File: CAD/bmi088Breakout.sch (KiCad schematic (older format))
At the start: 8 parts, among them J1 Conn_01x04_Male, U1 BMI088

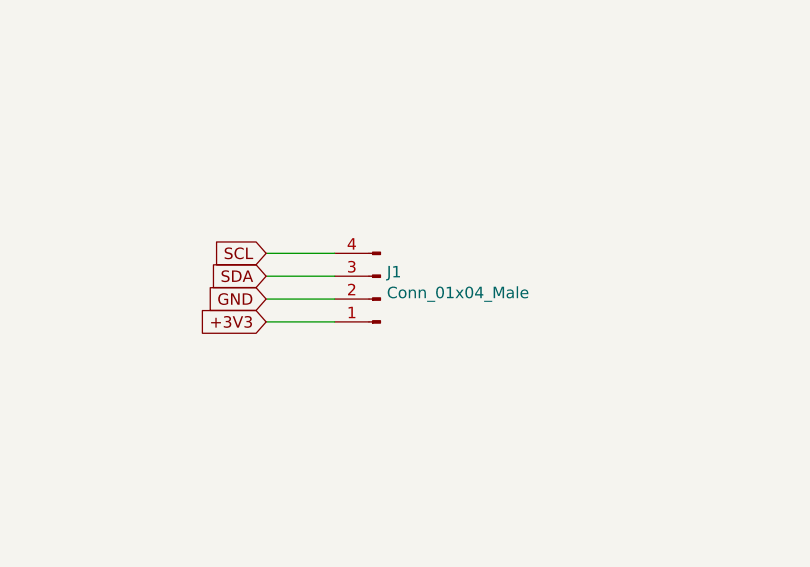
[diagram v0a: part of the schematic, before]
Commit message: added castellated holes to board
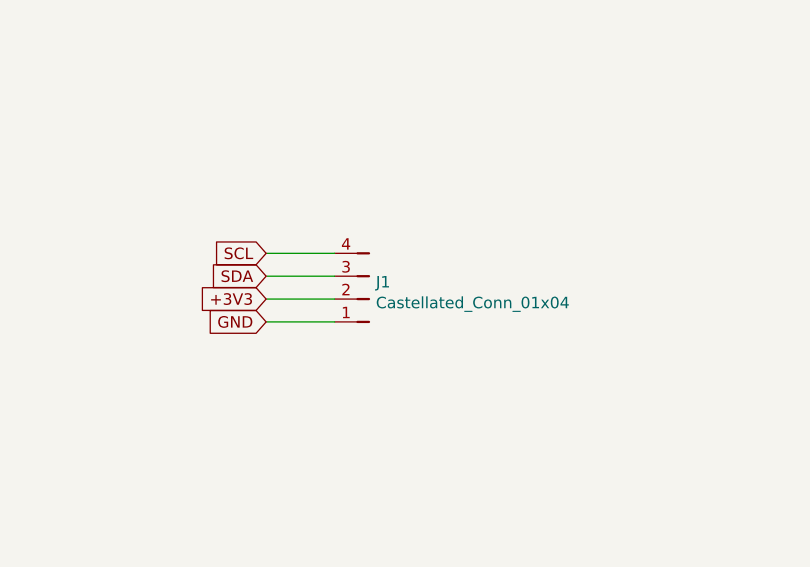
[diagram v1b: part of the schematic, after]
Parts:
- removed J1: Conn_01x04_Male, Connector_PinHeader_2.54mm:PinHeader_1x04_P2.54mm_Vertical, symbol Connector:Conn_01x04_Male
- added J1: Castellated_Conn_01x04, DS-connectors:Castellated_PinHeader_01x04_P2.54mm_Vertical, symbol DS-connectors:Castellated_Conn_01x04
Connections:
- net +3V3: now also J1.2
- net GND: now also J1.1
- net SCL: now also J1.4
- net SDA: now also J1.3
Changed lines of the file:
@@
 Wire Wire Line
 	6250 3150 6250 3300
-$Comp
-L Connector:Conn_01x04_Male J1
-U 1 1 614B0AD0
-P 6000 5050
-F 0 "J1" H 5972 4932 50  0000 R CNN
-F 1 "Conn_01x04_Male" H 5972 5023 50  0000 R CNN
-F 2 "Connector_PinHeader_2.54mm:PinHeader_1x04_P2.54mm_Vertical" H 6000 5050 50  0001 C CNN
-F 3 "~" H 6000 5050 50  0001 C CNN
-	1    6000 5050
-	-1   0    0    1
-$EndComp
 Text GLabel 5500 4850 0    50   Input ~ 0
 SCL
@@
 SDA
 Text GLabel 5500 5050 0    50   Input ~ 0
++3V3
+Text GLabel 5500 5150 0    50   Input ~ 0
 GND
-Text GLabel 5500 5150 0    50   Input ~ 0
-+3V3
 Wire Wire Line
 	5500 5150 5800 5150
@@
 Wire Wire Line
 	5500 4950 5800 4950
+$Comp
+L DS-connectors:Castellated_Conn_01x04 J1
+U 1 1 61534104
+P 5950 5200
+F 0 "J1" H 5920 4976 50  0000 R CNN
+F 1 "Castellated_Conn_01x04" H 5920 5067 50  0000 R CNN
+F 2 "DS-connectors:Castellated_PinHeader_01x04_P2.54mm_Vertical" H 5950 5200 50  0001 C CNN
+F 3 "" H 5950 5200 50  0001 C CNN
+	1    5950 5200
+	-1   0    0    1
+$EndComp
 $EndSCHEMATC

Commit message: Add files via upload
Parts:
- added J2, J3: Castellated_Conn_01x01, DS-connectors:Castellated_PinHeader_01x01_P2.54mm_Vertical, symbol DS-connectors:Castellated_Conn_01x01
- C1, C2: footprint Capacitor_SMD:C_0603_1608Metric -> Capacitor_SMD:C_0805_2012Metric
- R1, R2, R3: footprint Resistor_SMD:R_0603_1608Metric -> Resistor_SMD:R_0805_2012Metric
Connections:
- net GND: now also J2.1, J3.1
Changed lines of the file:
@@
 F 0 "C1" H 2092 3146 50  0000 L CNN
 F 1 "0.1uF" H 2092 3055 50  0000 L CNN
-F 2 "Capacitor_SMD:C_0603_1608Metric" H 2000 3100 50  0001 C CNN
+F 2 "Capacitor_SMD:C_0805_2012Metric" H 2000 3100 50  0001 C CNN
 F 3 "~" H 2000 3100 50  0001 C CNN
 	1    2000 3100
@@
 F 0 "C2" H 2592 3146 50  0000 L CNN
 F 1 "0.1uF" H 2592 3055 50  0000 L CNN
-F 2 "Capacitor_SMD:C_0603_1608Metric" H 2500 3100 50  0001 C CNN
+F 2 "Capacitor_SMD:C_0805_2012Metric" H 2500 3100 50  0001 C CNN
 F 3 "~" H 2500 3100 50  0001 C CNN
 	1    2500 3100
@@
 F 0 "R3" H 3568 3146 50  0000 L CNN
 F 1 "4.7k" H 3568 3055 50  0000 L CNN
-F 2 "Resistor_SMD:R_0603_1608Metric" H 3500 3100 50  0001 C CNN
+F 2 "Resistor_SMD:R_0805_2012Metric" H 3500 3100 50  0001 C CNN
 F 3 "~" H 3500 3100 50  0001 C CNN
 	1    3500 3100
@@
 F 0 "R2" H 4068 3146 50  0000 L CNN
 F 1 "4..7k" H 4068 3055 50  0000 L CNN
-F 2 "Resistor_SMD:R_0603_1608Metric" H 4000 3100 50  0001 C CNN
+F 2 "Resistor_SMD:R_0805_2012Metric" H 4000 3100 50  0001 C CNN
 F 3 "~" H 4000 3100 50  0001 C CNN
 	1    4000 3100
@@
 F 0 "R1" V 4995 3150 50  0000 C CNN
 F 1 "4.7k" V 5086 3150 50  0000 C CNN
-F 2 "Resistor_SMD:R_0603_1608Metric" H 5200 3150 50  0001 C CNN
+F 2 "Resistor_SMD:R_0805_2012Metric" H 5200 3150 50  0001 C CNN
 F 3 "~" H 5200 3150 50  0001 C CNN
 	1    5200 3150
@@
 	-1   0    0    1
 $EndComp
+$Comp
+L DS-connectors:Castellated_Conn_01x01 J2
+U 1 1 61538F96
+P 5950 5450
+F 0 "J2" H 5920 5276 50  0000 R CNN
+F 1 "Castellated_Conn_01x01" H 5920 5367 50  0000 R CNN
+F 2 "DS-connectors:Castellated_PinHeader_01x01_P2.54mm_Vertical" H 5950 5450 50  0001 C CNN
+F 3 "" H 5950 5450 50  0001 C CNN
+	1    5950 5450
+	-1   0    0    1
+$EndComp
+$Comp
+L DS-connectors:Castellated_Conn_01x01 J3
+U 1 1 6153A973
+P 5950 5650
+F 0 "J3" H 5920 5476 50  0000 R CNN
+F 1 "Castellated_Conn_01x01" H 5920 5567 50  0000 R CNN
+F 2 "DS-connectors:Castellated_PinHeader_01x01_P2.54mm_Vertical" H 5950 5650 50  0001 C CNN
+F 3 "" H 5950 5650 50  0001 C CNN
+	1    5950 5650
+	-1   0    0    1
+$EndComp
+Wire Wire Line
+	5500 5300 5800 5300
+Text GLabel 5500 5300 0    50   Input ~ 0
+GND
+Wire Wire Line
+	5800 5500 5500 5500
+Text GLabel 5500 5500 0    50   Input ~ 0
+GND
 $EndSCHEMATC
